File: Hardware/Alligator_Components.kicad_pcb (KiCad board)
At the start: 4 copper layers, 60 x 110 mm, 122 parts, among them J1 SWD_Header, J2 Eurorack_10_pin_power, J3 Conn_01x08_Male, J4 Conn_01x08_Male, J5 Conn_01x08_Male, J6 Conn_01x08_Male, J7 USB_B_Micro, U1 STM32H743ZITx, U2 IS42S16400J-xC, U3 PCM5100APW, U4 SSI2164, U5 MCP6004, U6 MCP6004, U7 TL074, U8 LM1117-3.3, Y1 8MHz 20pF

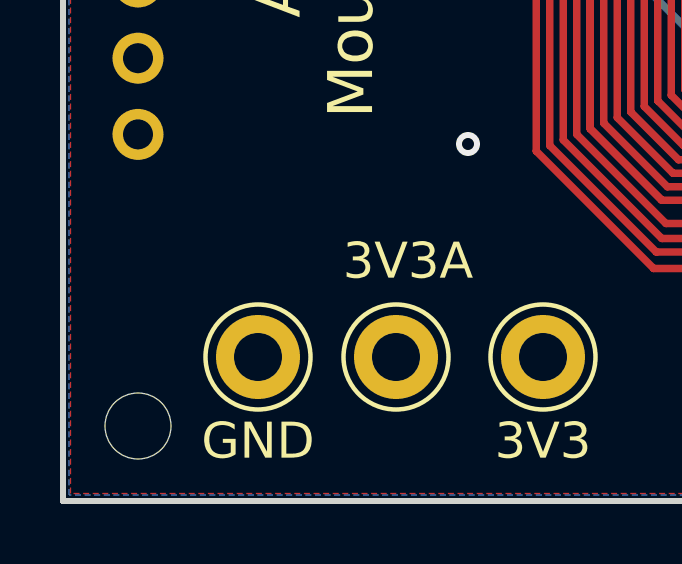
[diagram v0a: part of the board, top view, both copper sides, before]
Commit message: Completed first draft of Panel PCB
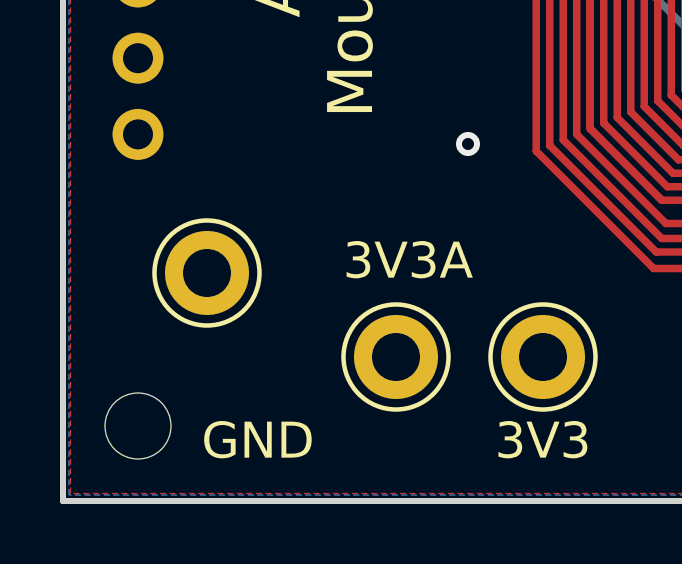
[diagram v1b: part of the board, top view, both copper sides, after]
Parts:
- moved TP1 3.28 mm to (104.8, 152.4)
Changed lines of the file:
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@@
     (0 F.Cu signal)
     (1 Ground.Fill power hide)
-    (2 Power.Rails power)
+    (2 Power.Rails power hide)
     (31 B.Cu signal)
     (32 B.Adhes user)
@@
   )
   (module Measurement_Points:Test_Point_Keystone_5005-5009_Compact (layer F.Cu)
-    (at 106.5 155.2)
+    (at 104.8 152.4)
     (descr "Keystone Miniature THM Test Point 5005-5009, http://www.keyelco.com/product-pdf.cfm?p=1314")
     (tags "Through Hole Mount Test Points")
